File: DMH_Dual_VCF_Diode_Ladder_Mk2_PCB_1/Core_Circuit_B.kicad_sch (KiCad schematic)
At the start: 41 parts, among them J20 Conn_01x04_PinHeader, SW4 SW_SPDT, SW5 SW_SPDT, SW6 SW_SPDT, U4 TL074, U6 TL074

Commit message: Corrected pin header footprint assignments
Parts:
- J20: footprint Connector_PinHeader_2.54mm:PinHeader_1x10_P2.54mm_Vertical -> Connector_PinSocket_2.54mm:PinSocket_1x04_P2.54mm_Vertical
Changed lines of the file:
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@@
 			)
 		)
-		(property "Footprint" "Connector_PinHeader_2.54mm:PinHeader_1x10_P2.54mm_Vertical"
+		(property "Footprint" "Connector_PinSocket_2.54mm:PinSocket_1x04_P2.54mm_Vertical"
 			(at 74.93 41.91 0)
 			(effects
@@
 			)
 		)
-		(property "Footprint" "Connector_PinHeader_2.54mm:PinHeader_1x10_P2.54mm_Vertical"
+		(property "Footprint" "Connector_PinSocket_2.54mm:PinSocket_1x04_P2.54mm_Vertical"
 			(at 93.98 41.91 0)
 			(effects
@@
 			)
 		)
-		(property "Footprint" "Connector_PinHeader_2.54mm:PinHeader_1x10_P2.54mm_Vertical"
+		(property "Footprint" "Connector_PinSocket_2.54mm:PinSocket_1x04_P2.54mm_Vertical"
 			(at 143.51 119.38 0)
 			(effects
@@
 			)
 		)
-		(property "Footprint" "Connector_PinHeader_2.54mm:PinHeader_1x10_P2.54mm_Vertical"
+		(property "Footprint" "Connector_PinSocket_2.54mm:PinSocket_1x04_P2.54mm_Vertical"
 			(at 146.05 81.28 0)
 			(effects

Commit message: PCB1 component placement in progress
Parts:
- J20: footprint Connector_PinSocket_2.54mm:PinSocket_1x04_P2.54mm_Vertical -> Connector_PinHeader_2.54mm:PinHeader_1x04_P2.54mm_Vertical
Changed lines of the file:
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@@
 			)
 		)
-		(property "Footprint" "Connector_PinSocket_2.54mm:PinSocket_1x04_P2.54mm_Vertical"
+		(property "Footprint" "Connector_PinHeader_2.54mm:PinHeader_1x04_P2.54mm_Vertical"
 			(at 74.93 41.91 0)
 			(effects
@@
 			)
 		)
-		(property "Footprint" "Connector_PinSocket_2.54mm:PinSocket_1x04_P2.54mm_Vertical"
+		(property "Footprint" "Connector_PinHeader_2.54mm:PinHeader_1x04_P2.54mm_Vertical"
 			(at 93.98 41.91 0)
 			(effects
@@
 			)
 		)
-		(property "Footprint" "Connector_PinSocket_2.54mm:PinSocket_1x04_P2.54mm_Vertical"
+		(property "Footprint" "Connector_PinHeader_2.54mm:PinHeader_1x04_P2.54mm_Vertical"
 			(at 143.51 119.38 0)
 			(effects
@@
 			)
 		)
-		(property "Footprint" "Connector_PinSocket_2.54mm:PinSocket_1x04_P2.54mm_Vertical"
+		(property "Footprint" "Connector_PinHeader_2.54mm:PinHeader_1x04_P2.54mm_Vertical"
 			(at 146.05 81.28 0)
 			(effects

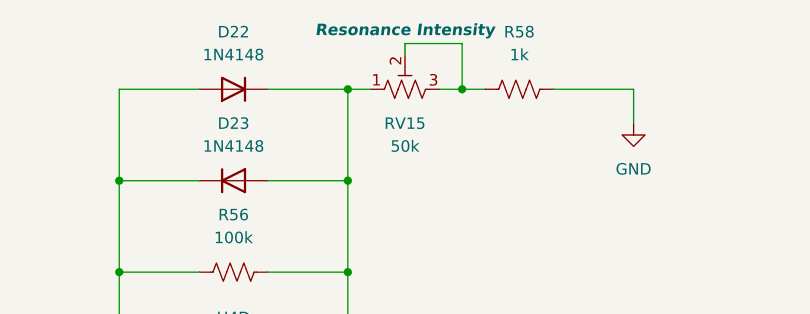
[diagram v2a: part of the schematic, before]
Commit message: Added trim pot functions to silkscreen
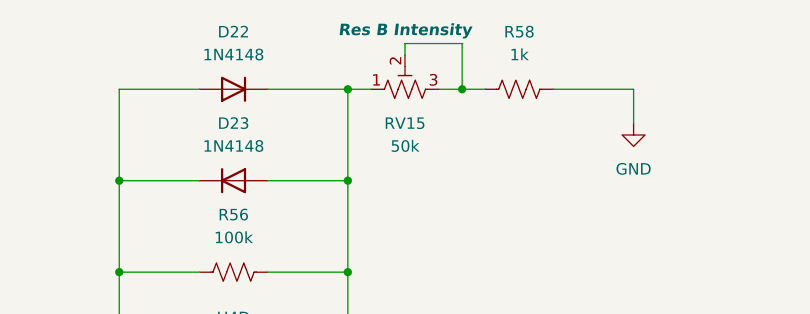
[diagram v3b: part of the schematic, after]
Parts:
- RV15: Function Resonance Intensity -> Res B Intensity
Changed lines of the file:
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@@
 			)
 		)
-		(property "Function" "Resonance Intensity"
+		(property "Function" "Res B Intensity"
 			(at 209.55 23.876 90)
 			(effects

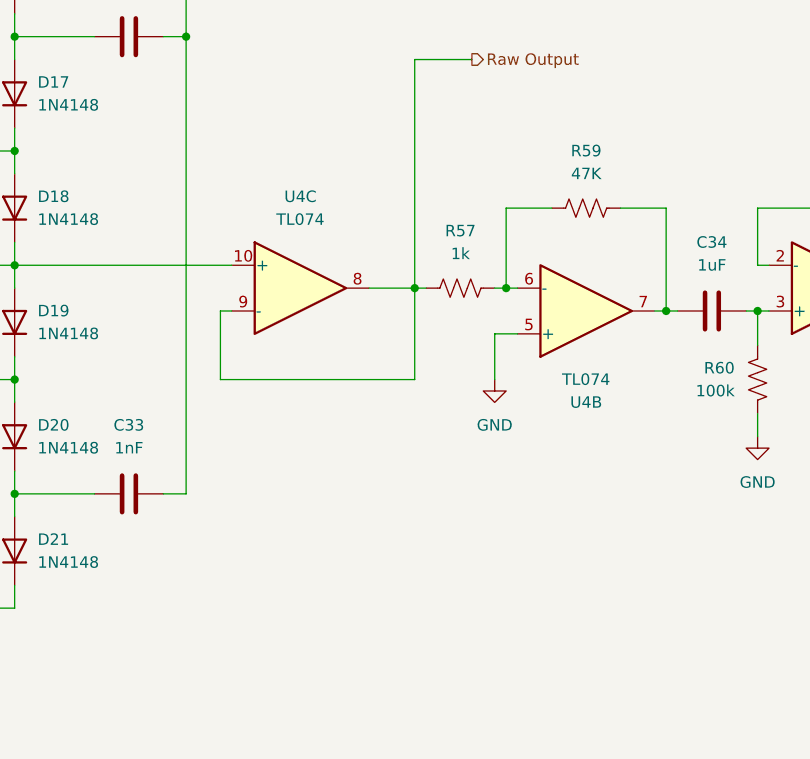
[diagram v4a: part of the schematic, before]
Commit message: Updated schematic during validation
- Changed Resonance B VCA gain resistors to 2k2
- Added range limiting resistors to all Cutoff pots
- Moved 48x gain to non-inverting opamp stage in Core Circuit to allow for Resonance voltage control.
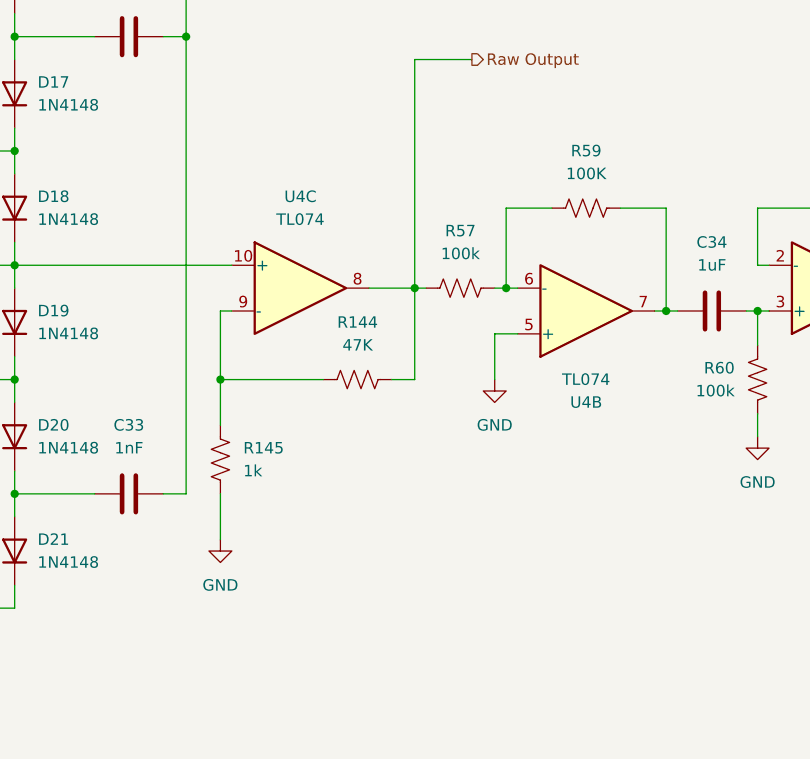
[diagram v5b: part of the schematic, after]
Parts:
- added R144: 47K, Resistor_THT:R_Axial_DIN0207_L6.3mm_D2.5mm_P7.62mm_Horizontal, symbol Device:R_US
- added R145: 1k, Resistor_THT:R_Axial_DIN0207_L6.3mm_D2.5mm_P7.62mm_Horizontal, symbol Device:R_US
- R57: value 1k -> 100k
- R59: value 47K -> 100K
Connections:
- net GND: now also R145.1
- net Raw Output: now also R144.2; no longer U4.9 (-)
- new net: R144.1, R145.2, U4.9 (-)
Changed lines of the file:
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@@
 	)
 	(junction
+		(at 181.61 111.76)
+		(diameter 0)
+		(color 0 0 0 0)
+	)
+	(junction
 		(at 177.8 40.64)
 		(diameter 0)
@@
 	(wire
 		(pts
+			(xy 181.61 124.46) (xy 181.61 129.54)
+		)
+		(stroke
+			(width 0)
+			(type default)
+		)
+	)
+	(wire
+		(pts
 			(xy 143.51 99.06) (xy 143.51 114.3)
 		)
@@
 	(wire
 		(pts
+			(xy 181.61 111.76) (xy 181.61 116.84)
+		)
+		(stroke
+			(width 0)
+			(type default)
+		)
+	)
+	(wire
+		(pts
 			(xy 240.03 104.14) (xy 241.3 104.14)
 		)
@@
 	(wire
 		(pts
-			(xy 181.61 111.76) (xy 203.2 111.76)
+			(xy 181.61 111.76) (xy 193.04 111.76)
 		)
 		(stroke
@@
 	(wire
 		(pts
+			(xy 200.66 111.76) (xy 203.2 111.76)
+		)
+		(stroke
+			(width 0)
+			(type default)
+		)
+	)
+	(wire
+		(pts
 			(xy 267.97 101.6) (xy 270.51 101.6)
 		)
@@
 	)
 	(symbol
+		(lib_id "Device:R_US")
+		(at 196.85 111.76 90)
+		(unit 1)
+		(exclude_from_sim no)
+		(in_bom yes)
+		(on_board yes)
+		(dnp no)
+		(fields_autoplaced yes)
+		(property "Reference" "R144"
+			(at 196.85 105.41 90)
+			(effects
+				(font
+					(size 1.27 1.27)
+				)
+			)
+		)
+		(property "Value" "47K"
+			(at 196.85 107.95 90)
+			(effects
+				(font
+					(size 1.27 1.27)
+				)
+			)
+		)
+		(property "Footprint" "Resistor_THT:R_Axial_DIN0207_L6.3mm_D2.5mm_P7.62mm_Horizontal"
+			(at 197.104 110.744 90)
+			(effects
+				(font
+					(size 1.27 1.27)
+				)
+				(hide yes)
+			)
+		)
+		(property "Datasheet" "~"
+			(at 196.85 111.76 0)
+			(effects
+				(font
+					(size 1.27 1.27)
+				)
+				(hide yes)
+			)
+		)
+		(property "Description" "Resistor, US symbol"
+			(at 196.85 111.76 0)
+			(effects
+				(font
+					(size 1.27 1.27)
+				)
+				(hide yes)
+			)
+		)
+		(pin "2"
+		)
+		(pin "1"
+		)
+		(instances
+			(project "DMH_Dual_VCF_Diode_Ladder_Mk2_PCB_1"
+				(path "/58f4306d-5387-4983-bb08-41a2313fd315/5770dcd3-eb9e-472f-b743-1e3eb22ed082"
+					(reference "R144")
+					(unit 1)
+				)
+			)
+		)
+	)
+	(symbol
 		(lib_id "Device:C")
 		(at 152.4 111.76 90)
@@
 	)
 	(symbol
+		(lib_id "power:GND")
+		(at 181.61 129.54 0)
+		(unit 1)
+		(exclude_from_sim no)
+		(in_bom yes)
+		(on_board yes)
+		(dnp no)
+		(fields_autoplaced yes)
+		(property "Reference" "#PWR0110"
+			(at 181.61 135.89 0)
+			(effects
+				(font
+					(size 1.27 1.27)
+				)
+				(hide yes)
+			)
+		)
+		(property "Value" "GND"
+			(at 181.61 134.62 0)
+			(effects
+				(font
+					(size 1.27 1.27)
+				)
+			)
+		)
+		(property "Footprint" ""
+			(at 181.61 129.54 0)
+			(effects
+				(font
+					(size 1.27 1.27)
+				)
+				(hide yes)
+			)
+		)
+		(property "Datasheet" ""
+			(at 181.61 129.54 0)
+			(effects
+				(font
+					(size 1.27 1.27)
+				)
+				(hide yes)
+			)
+		)
+		(property "Description" "Power symbol creates a global label with name \"GND\" , ground"
+			(at 181.61 129.54 0)
+			(effects
+				(font
+					(size 1.27 1.27)
+				)
+				(hide yes)
+			)
+		)
+		(pin "1"
+		)
+		(instances
+			(project "DMH_Dual_VCF_Diode_Ladder_Mk2_PCB_1"
+				(path "/58f4306d-5387-4983-bb08-41a2313fd315/5770dcd3-eb9e-472f-b743-1e3eb22ed082"
+					(reference "#PWR0110")
+					(unit 1)
+				)
+			)
+		)
+	)
+	(symbol
 		(lib_id "Diode:1N4148")
 		(at 158.75 118.11 90)
@@
 			)
 		)
-		(property "Value" "47K"
+		(property "Value" "100K"
 			(at 222.25 88.9 90)
 			(effects
@@
 	(symbol
 		(lib_id "Device:R_US")
+		(at 181.61 120.65 180)
+		(unit 1)
+		(exclude_from_sim no)
+		(in_bom yes)
+		(on_board yes)
+		(dnp no)
+		(fields_autoplaced yes)
+		(property "Reference" "R145"
+			(at 184.15 119.3799 0)
+			(effects
+				(font
+					(size 1.27 1.27)
+				)
+				(justify right)
+			)
+		)
+		(property "Value" "1k"
+			(at 184.15 121.9199 0)
+			(effects
+				(font
+					(size 1.27 1.27)
+				)
+				(justify right)
+			)
+		)
+		(property "Footprint" "Resistor_THT:R_Axial_DIN0207_L6.3mm_D2.5mm_P7.62mm_Horizontal"
+			(at 180.594 120.396 90)
+			(effects
+				(font
+					(size 1.27 1.27)
+				)
+				(hide yes)
+			)
+		)
+		(property "Datasheet" "~"
+			(at 181.61 120.65 0)
+			(effects
+				(font
+					(size 1.27 1.27)
+				)
+				(hide yes)
+			)
+		)
+		(property "Description" "Resistor, US symbol"
+			(at 181.61 120.65 0)
+			(effects
+				(font
+					(size 1.27 1.27)
+				)
+				(hide yes)
+			)
+		)
+		(pin "2"
+		)
+		(pin "1"
+		)
+		(instances
+			(project "DMH_Dual_VCF_Diode_Ladder_Mk2_PCB_1"
+				(path "/58f4306d-5387-4983-bb08-41a2313fd315/5770dcd3-eb9e-472f-b743-1e3eb22ed082"
+					(reference "R145")
+					(unit 1)
+				)
+			)
+		)
+	)
+	(symbol
+		(lib_id "Device:R_US")
 		(at 100.33 60.96 90)
 		(unit 1)
@@
 			)
 		)
-		(property "Value" "1k"
+		(property "Value" "100k"
 			(at 208.28 97.79 90)
 			(effects

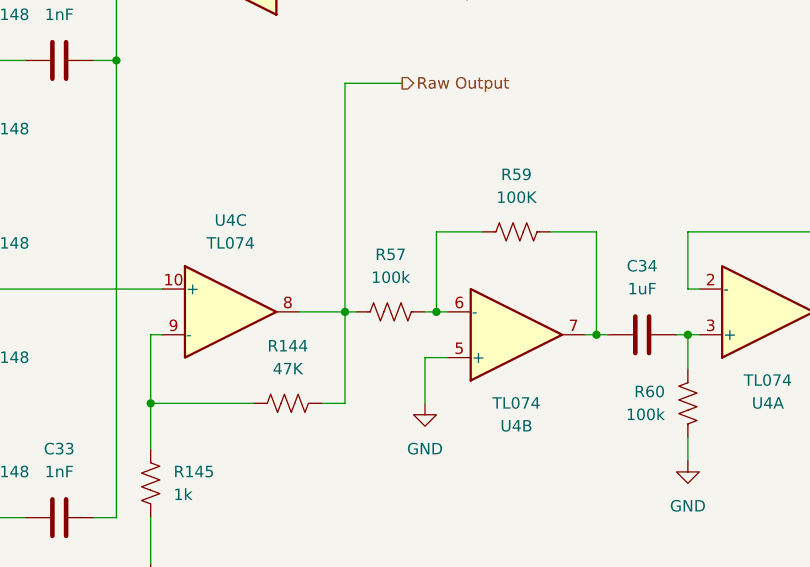
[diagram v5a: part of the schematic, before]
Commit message: Updated various resistor values
... and deleted all VCAs output 1k resistors
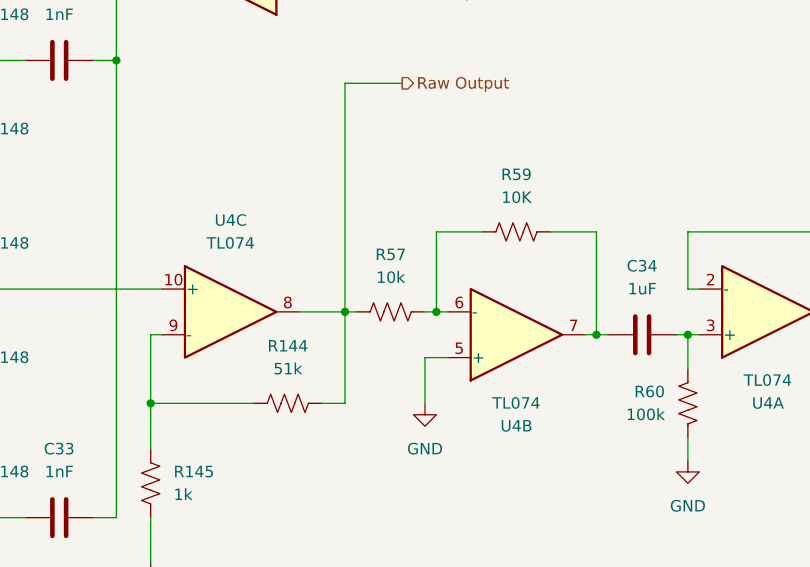
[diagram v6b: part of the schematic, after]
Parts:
- R144: value 47K -> 51k
- R57: value 100k -> 10k
- R59: value 100K -> 10K
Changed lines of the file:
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@@
 			)
 		)
-		(property "Value" "47K"
+		(property "Value" "51k"
 			(at 196.85 107.95 90)
 			(effects
@@
 			)
 		)
-		(property "Value" "100K"
+		(property "Value" "10K"
 			(at 222.25 88.9 90)
 			(effects
@@
 			)
 		)
-		(property "Value" "100k"
+		(property "Value" "10k"
 			(at 208.28 97.79 90)
 			(effects

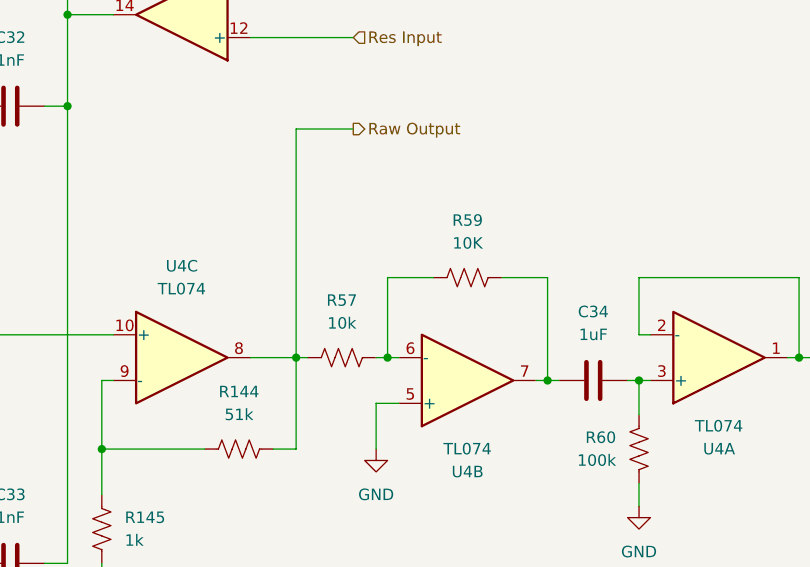
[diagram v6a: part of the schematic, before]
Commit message: Added V/oct calib to CV3 B
And changed output inverter stage resistors back to 100k
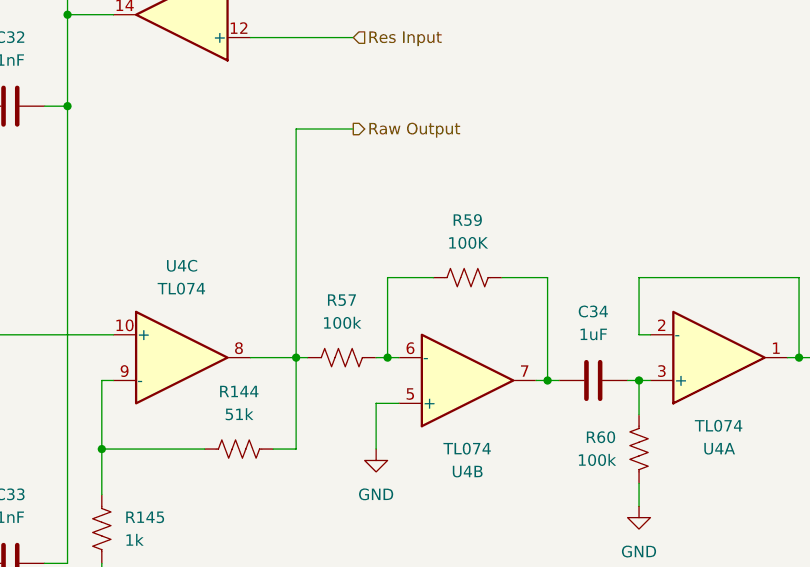
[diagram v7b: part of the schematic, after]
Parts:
- R57: value 10k -> 100k
- R59: value 10K -> 100K
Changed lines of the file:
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@@
 			)
 		)
-		(property "Value" "10K"
+		(property "Value" "100K"
 			(at 222.25 88.9 90)
 			(effects
@@
 			)
 		)
-		(property "Value" "10k"
+		(property "Value" "100k"
 			(at 208.28 97.79 90)
 			(effects

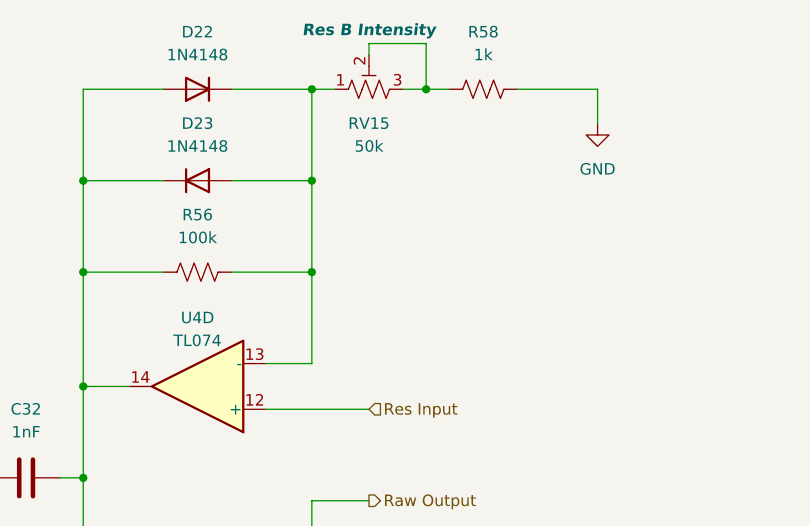
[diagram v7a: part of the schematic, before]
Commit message: Moved Res Int and CV3 V/Oct trims to front panel
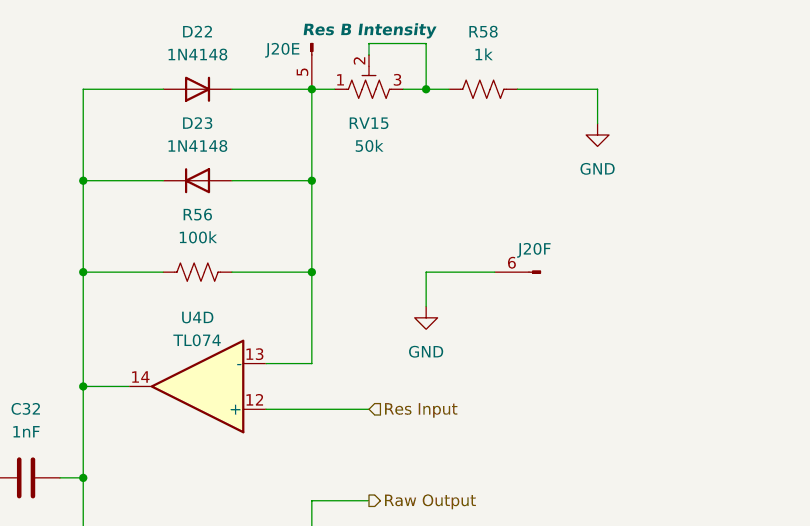
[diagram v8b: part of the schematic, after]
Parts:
- added unit 6 of J20
- added unit 5 of J20
- J20: value Conn_01x04_PinHeader -> Conn_01x06_PinHeader; footprint Connector_PinHeader_2.54mm:PinHeader_1x04_P2.54mm_Vertical -> (none); symbol SynthStuff:Conn_01x04_PinHeader -> SynthStuff:Conn_01x06_PinHeader
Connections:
- net GND: now also J20.6 (Pin_6)
- net at D22.1 (K), D23.2 (A), R56.2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: now also J20.5 (Pin_5)
